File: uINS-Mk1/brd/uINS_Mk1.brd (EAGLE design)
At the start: 38.1 x 38.1 mm, 13 parts

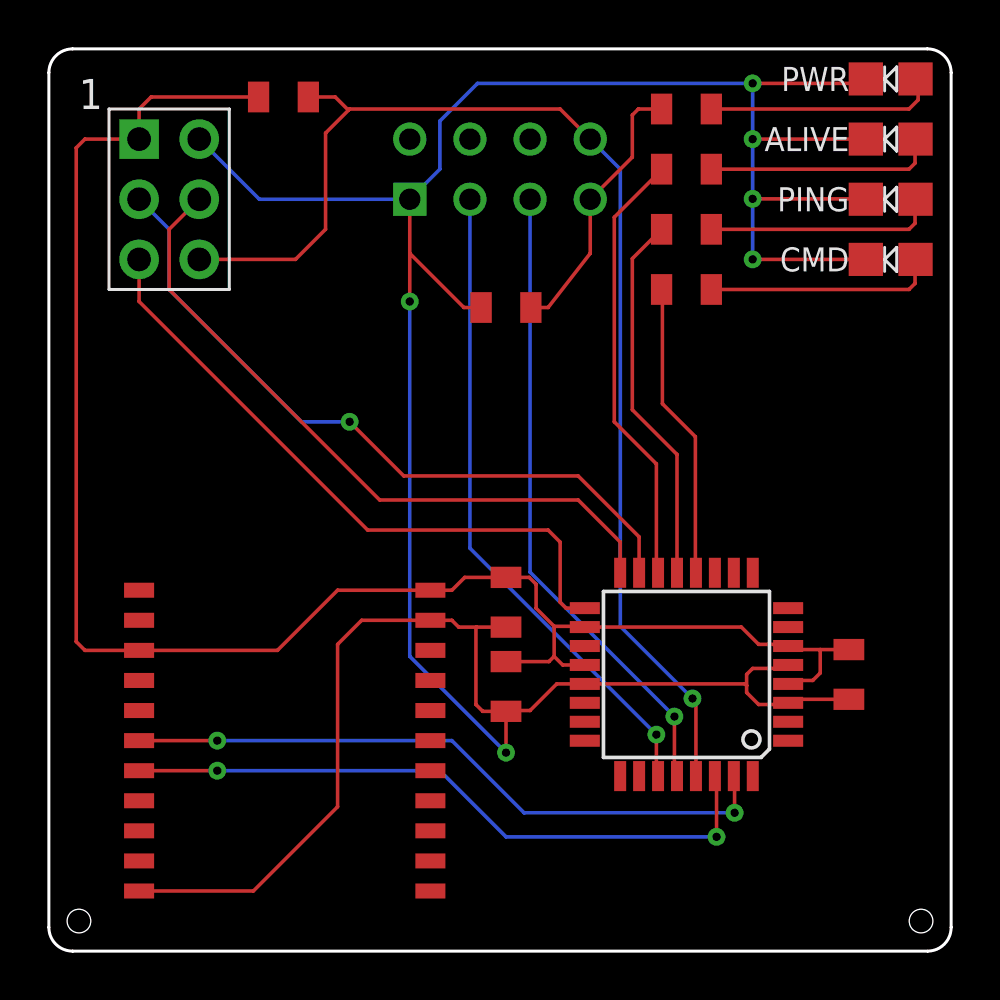
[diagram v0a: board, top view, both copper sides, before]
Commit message: updated board templates and modified existing boards to use the mk2 templates.
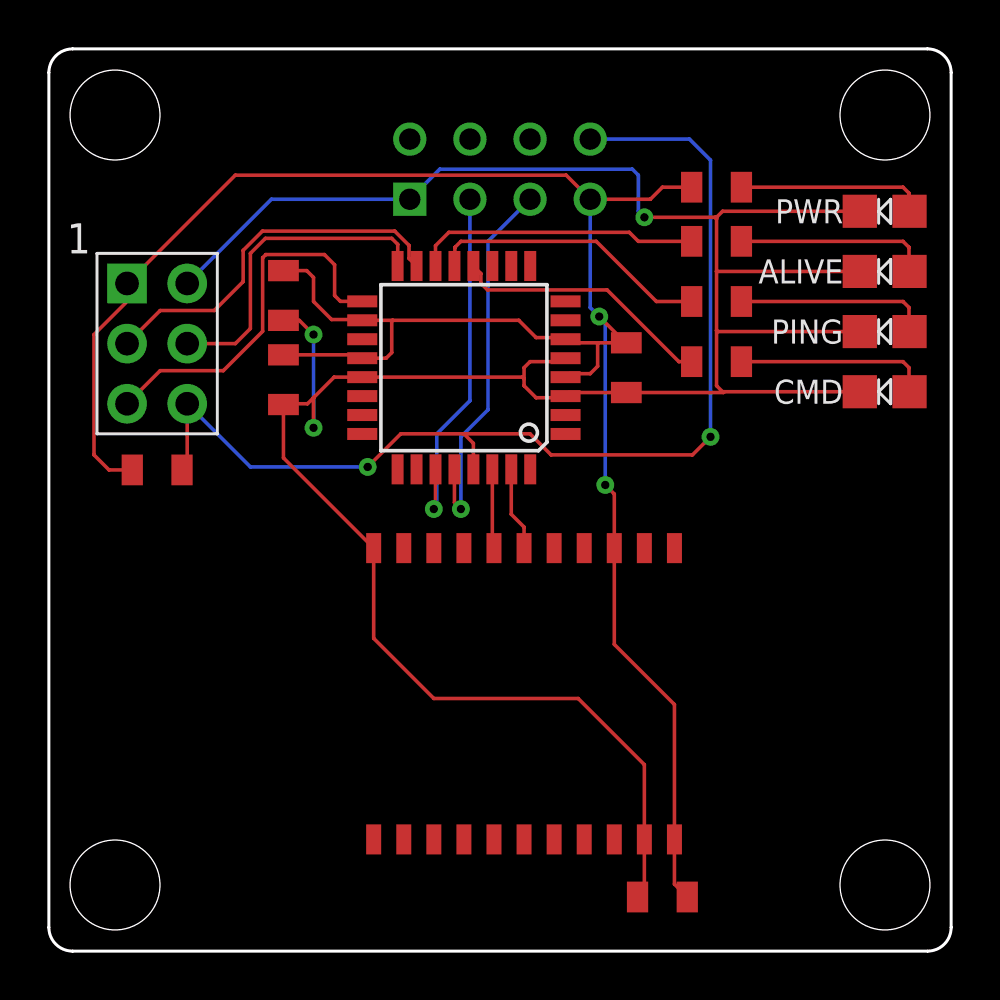
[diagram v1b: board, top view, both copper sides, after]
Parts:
- U$3: value (none) -> 100nF
- U$6, U$7, U$8, U$9: value (none) -> 10k
- moved U$13 25.8 mm to (25.9, 2.29)
- moved U_INS 19.7 mm to (12.4, 18.3), turned to 270 degrees
- moved U$10 16.6 mm to (4.57, 20.3)
- moved U$11 16.0 mm to (9.91, 27.7)
- moved U$4 16.0 mm to (17.5, 24.6)
- moved U$12 16.0 mm to (24.4, 24.6)
- moved U$3 16.0 mm to (9.91, 24.1)
- moved U$5 6.12 mm to (3.30, 28.2)
- moved U$6 3.54 mm to (28.2, 32.3)
- moved U$7 3.30 mm to (28.2, 30.0)
- moved U$8 3.30 mm to (28.2, 27.4)
- moved U$9 3.30 mm to (28.2, 24.9)
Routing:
- net GPS_TX: track 28.1 -> 3.36 mm, vias 2 -> 0
- net GPS_RX: track 28.0 -> 3.55 mm, vias 2 -> 0
- net MISO: track 29.1 -> 13.6 mm
- net GND: track 132.0 -> 117.3 mm, vias 6 -> 3
- net MOSI: track 30.0 -> 15.9 mm, vias 1 -> 0
- net SDA: track 27.6 -> 15.4 mm
- net SCK: track 27.5 -> 15.9 mm
- net SCL: track 26.9 -> 16.1 mm
- net PWR: track 85.0 -> 93.8 mm, vias 0 -> 2
- net RESET: track 52.7 -> 46.1 mm, vias 1 -> 2
- net ALIVE: track 18.6 -> 12.1 mm
- net PING: track 15.8 -> 12.0 mm
- net N$3: track 9.82 -> 7.95 mm
- net N$8: track 9.73 -> 8.21 mm
- net N$7: track 9.73 -> 8.21 mm
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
